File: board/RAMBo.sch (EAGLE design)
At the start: 307 parts, among them Q1 PSMN7R0-60YS, Q2 PSMN7R0-60YS, Q3 PSMN7R0-60YS, Q4 IRLML6346TRPBF, Q5 PSMN7R0-60YS, Q8 IRLML6346TRPBF, U1 ATMEGA32U2-MUR, U10 ADUM7441, U2 ATMEGA2560-16AU, U3 LM22675, U4 AD5206, U5 A4982, U6 A4982, U7 A4982, U8 A4982, U9 A4982, X1 C-GRID-02-70543, X10 C-GRID-04-70543, X11 MSTBV10, X12 SPI, X13 EXT-2, X14 C-GRID-04-70543, X15 C-GRID-04-70543, X16 32u2 EXT, X17 3x2M, X18 3x2M, X2 USB B-TH, X20 MX1, X21 C-GRID-03-70543, X22 C-GRID-03-70543, X23 C-GRID-03-70543, X24 C-GRID-03-70543, X25 C-GRID-03-70543, X26 C-GRID-03-70543, X27 C-GRID-02-70543, X28 C-GRID-02-70543, X29 C-GRID-02-70543, X3 C-GRID-02-70543, X30 C-GRID-02-70543, X31 MX2, X32 MX3, X33 MSTBA6, X34 PWM_EXT, X39 M05X2PTH, X4 C-GRID-04-70543, X40 Analog, X5 C-GRID-02-70543, X6 C-GRID-04-70543, X7 C-GRID-04-70543, X8 C-GRID-04-70543, X9 C-GRID-02-70543, Y1 16MHz KX-7, Y2 16MHz KX-7

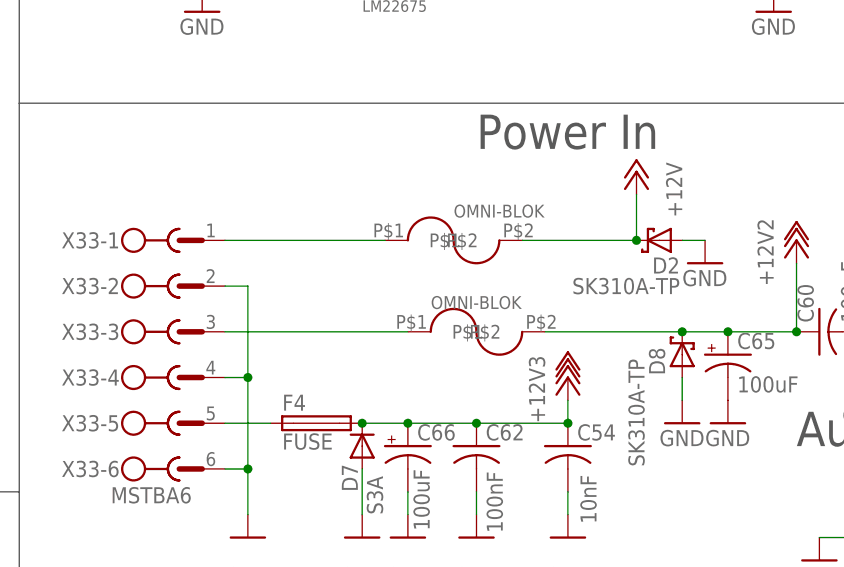
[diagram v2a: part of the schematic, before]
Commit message: Add ferrite beads to motor + htr/logic pwr input
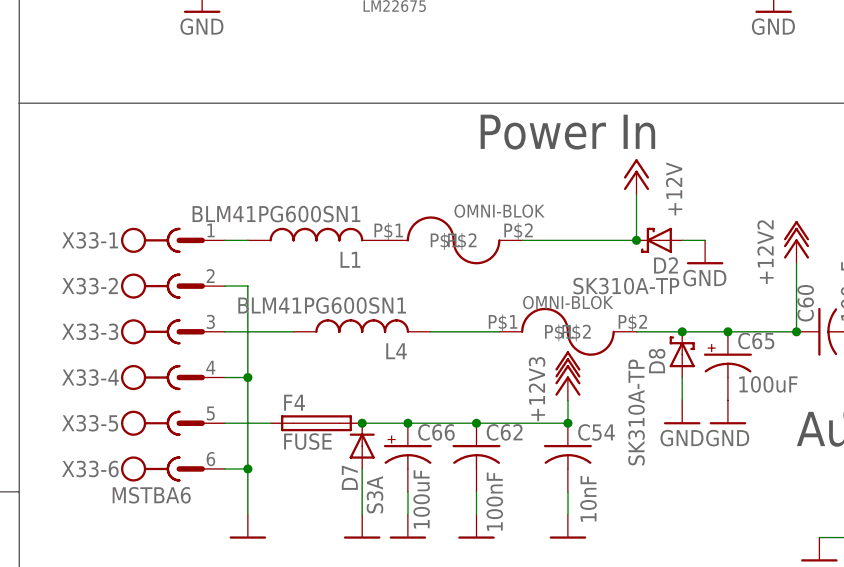
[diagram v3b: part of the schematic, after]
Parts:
- added L1, L4: BLM41PG600SN1, rcl:L-USL1806
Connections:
- new net N$172: F2.P$1, L1.2
- new net N$174: L4.1, X33-3.1
- net N$13: now also L1.1; no longer F2.P$1
- net N$14: now also L4.2; no longer X33-3.1
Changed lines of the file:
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@@
 <part name="GND107" library="supply1" deviceset="GND" device=""/>
 <part name="GND108" library="supply1" deviceset="GND" device=""/>
+<part name="L1" library="rcl" deviceset="L-US" device="L1806" value="BLM41PG600SN1"/>
+<part name="L4" library="rcl" deviceset="L-US" device="L1806" value="BLM41PG600SN1"/>
 </parts>
 <sheets>
@@
 <instance part="Q3" gate="G$1" x="596.9" y="198.12"/>
 <instance part="Q5" gate="G$1" x="546.1" y="152.4"/>
-<instance part="F3" gate="G$1" x="698.5" y="246.38" smashed="yes">
-<attribute name="NAME" x="690.88" y="243.84" size="1.4224" layer="104"/>
-<attribute name="VALUE" x="693.42" y="248.92" size="1.4224" layer="96"/>
+<instance part="F3" gate="G$1" x="708.66" y="246.38" smashed="yes">
+<attribute name="NAME" x="701.04" y="243.84" size="1.4224" layer="104"/>
+<attribute name="VALUE" x="703.58" y="248.92" size="1.4224" layer="96"/>
 </instance>
 <instance part="F2" gate="G$1" x="695.96" y="256.54" smashed="yes">
@@
 <instance part="GND107" gate="1" x="457.2" y="10.16"/>
 <instance part="GND108" gate="1" x="358.14" y="86.36"/>
+<instance part="L1" gate="G$1" x="680.72" y="256.54" rot="R90"/>
+<instance part="L4" gate="G$1" x="685.8" y="246.38" rot="R90"/>
 </instances>
 <busses>
@@
 <pinref part="C60" gate="G$1" pin="1"/>
 <junction x="734.06" y="246.38"/>
-<wire x1="721.36" y1="246.38" x2="706.12" y2="246.38" width="0.1524" layer="91"/>
+<wire x1="721.36" y1="246.38" x2="716.28" y2="246.38" width="0.1524" layer="91"/>
 <pinref part="D8" gate="G$1" pin="C"/>
 <junction x="721.36" y="246.38"/>
@@
 <net name="N$13" class="0">
 <segment>
-<pinref part="F2" gate="G$1" pin="P$1"/>
 <pinref part="X33" gate="-1" pin="1"/>
-<wire x1="688.34" y1="256.54" x2="670.56" y2="256.54" width="0.1524" layer="91"/>
+<pinref part="L1" gate="G$1" pin="1"/>
+<wire x1="673.1" y1="256.54" x2="670.56" y2="256.54" width="0.1524" layer="91"/>
 </segment>
 </net>
@@
 <segment>
 <pinref part="F3" gate="G$1" pin="P$1"/>
-<pinref part="X33" gate="-3" pin="1"/>
-<wire x1="690.88" y1="246.38" x2="670.56" y2="246.38" width="0.1524" layer="91"/>
+<wire x1="701.04" y1="246.38" x2="693.42" y2="246.38" width="0.1524" layer="91"/>
+<pinref part="L4" gate="G$1" pin="2"/>
 </segment>
 </net>
@@
 </segment>
 </net>
+<net name="N$172" class="0">
+<segment>
+<pinref part="F2" gate="G$1" pin="P$1"/>
+<pinref part="L1" gate="G$1" pin="2"/>
+</segment>
+</net>
+<net name="N$174" class="0">
+<segment>
+<pinref part="X33" gate="-3" pin="1"/>
+<pinref part="L4" gate="G$1" pin="1"/>
+<wire x1="678.18" y1="246.38" x2="670.56" y2="246.38" width="0.1524" layer="91"/>
+</segment>
+</net>
